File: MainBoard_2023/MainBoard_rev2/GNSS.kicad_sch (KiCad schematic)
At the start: 12 parts

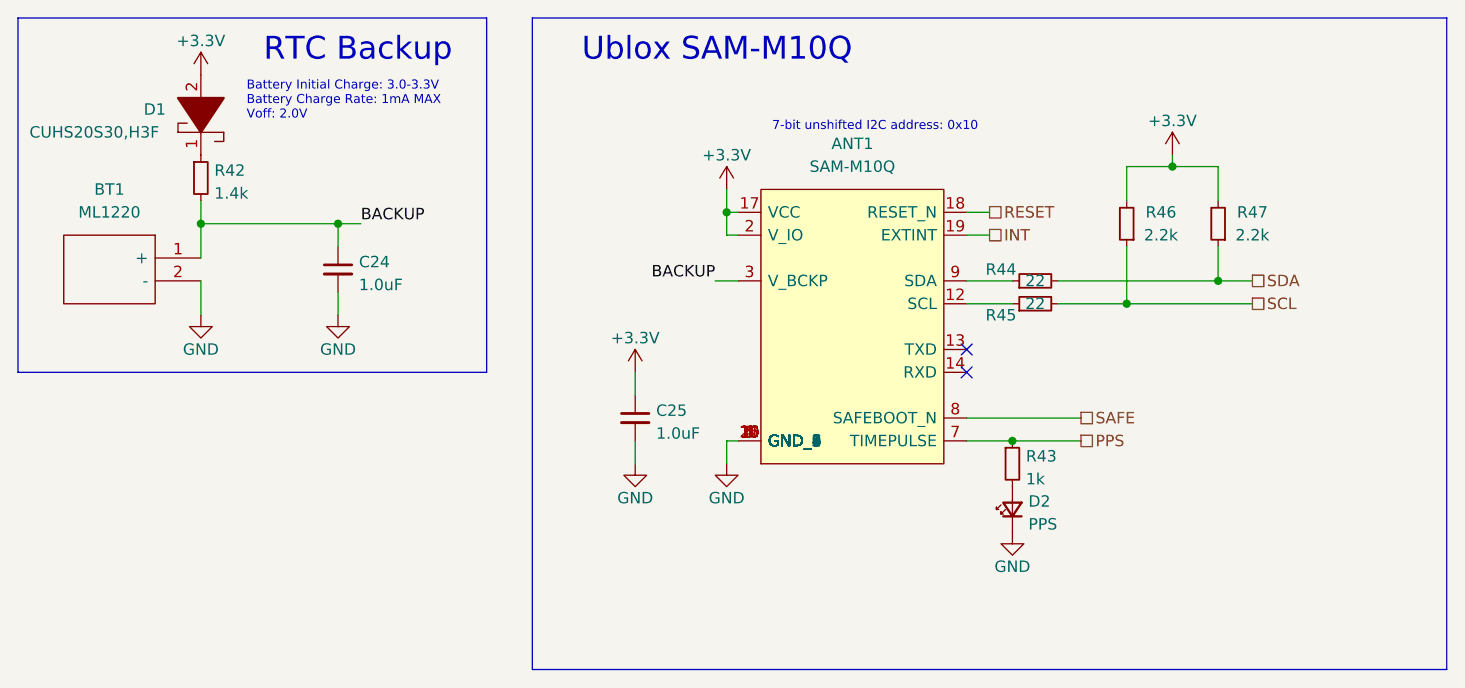
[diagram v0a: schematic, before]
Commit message: PCBファイルを作成
3Dモデルを割り当て　ブロックタイプエミフィルのパッドを小さくした
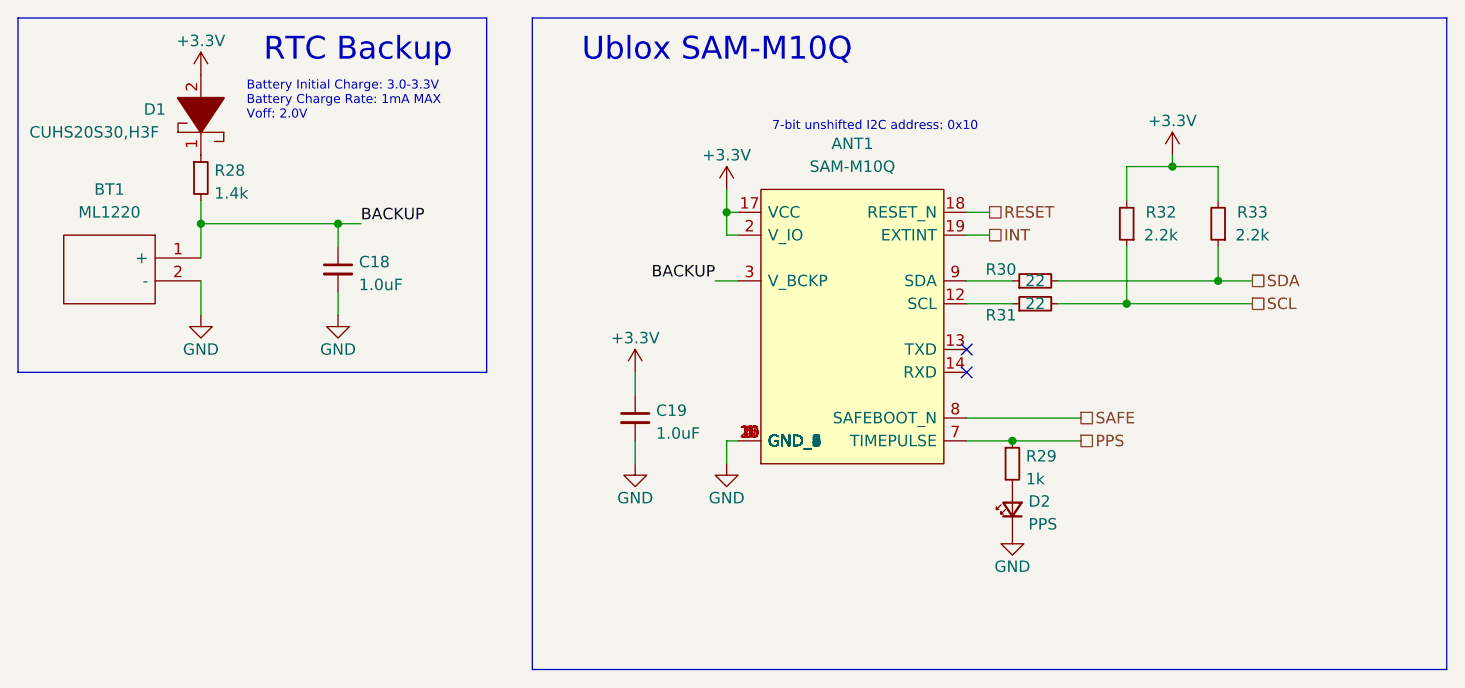
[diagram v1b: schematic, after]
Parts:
- renumbered C24 to C18, C25 to C19, R42 to R28, R43 to R29, R44 to R30, R45 to R31, R46 to R32, R47 to R33
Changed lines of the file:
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@@
   (symbol (lib_id "power:+3.3V") (at 195.58 72.39 0) (unit 1)
     (in_bom yes) (on_board yes)
-    (property "Reference" "#PWR0127" (id 0) (at 195.58 76.2 0)
+    (property "Reference" "#PWR084" (id 0) (at 195.58 76.2 0)
       (effects (font (size 1.27 1.27)) hide)
     )
@@
   (symbol (lib_id "Device:R_Small") (at 180.34 88.9 90) (unit 1)
     (in_bom yes) (on_board yes)
-    (property "Reference" "R45" (id 0) (at 176.53 90.17 90))
+    (property "Reference" "R31" (id 0) (at 176.53 90.17 90))
     (property "Value" "22" (id 1) (at 180.34 88.9 90))
     (property "Footprint" "Resistor_SMD:R_0603_1608Metric_Pad0.98x0.95mm_HandSolder" (id 2) (at 180.34 88.9 0)
@@
   (symbol (lib_id "power:+3.3V") (at 135.89 96.52 0) (unit 1)
     (in_bom yes) (on_board yes)
-    (property "Reference" "#PWR0122" (id 0) (at 135.89 100.33 0)
+    (property "Reference" "#PWR079" (id 0) (at 135.89 100.33 0)
       (effects (font (size 1.27 1.27)) hide)
     )
@@
   (symbol (lib_id "Device:R_Small") (at 200.66 80.01 180) (unit 1)
     (in_bom yes) (on_board yes)
-    (property "Reference" "R47" (id 0) (at 204.47 78.74 0))
+    (property "Reference" "R33" (id 0) (at 204.47 78.74 0))
     (property "Value" "2.2k" (id 1) (at 204.47 81.28 0))
     (property "Footprint" "Resistor_SMD:R_0603_1608Metric_Pad0.98x0.95mm_HandSolder" (id 2) (at 200.66 80.01 0)
@@
   (symbol (lib_id "power:GND") (at 135.89 106.68 0) (unit 1)
     (in_bom yes) (on_board yes)
-    (property "Reference" "#PWR0123" (id 0) (at 135.89 113.03 0)
+    (property "Reference" "#PWR080" (id 0) (at 135.89 113.03 0)
       (effects (font (size 1.27 1.27)) hide)
     )
@@
   (symbol (lib_id "Device:C_Small") (at 135.89 101.6 0) (unit 1)
     (in_bom yes) (on_board yes) (fields_autoplaced)
-    (property "Reference" "C25" (id 0) (at 138.2141 100.7716 0)
+    (property "Reference" "C19" (id 0) (at 138.2141 100.7716 0)
       (effects (font (size 1.27 1.27)) (justify left))
     )
@@
   (symbol (lib_id "Device:C_Small") (at 102.87 85.09 0) (unit 1)
     (in_bom yes) (on_board yes) (fields_autoplaced)
-    (property "Reference" "C24" (id 0) (at 105.1941 84.2616 0)
+    (property "Reference" "C18" (id 0) (at 105.1941 84.2616 0)
       (effects (font (size 1.27 1.27)) (justify left))
     )
@@
   (symbol (lib_id "power:+3.3V") (at 146.05 76.2 0) (unit 1)
     (in_bom yes) (on_board yes)
-    (property "Reference" "#PWR0124" (id 0) (at 146.05 80.01 0)
+    (property "Reference" "#PWR081" (id 0) (at 146.05 80.01 0)
       (effects (font (size 1.27 1.27)) hide)
     )
@@
   (symbol (lib_id "power:GND") (at 177.8 114.3 0) (unit 1)
     (in_bom yes) (on_board yes)
-    (property "Reference" "#PWR0126" (id 0) (at 177.8 120.65 0)
+    (property "Reference" "#PWR083" (id 0) (at 177.8 120.65 0)
       (effects (font (size 1.27 1.27)) hide)
     )
@@
   (symbol (lib_id "Device:R_Small") (at 87.63 74.93 0) (unit 1)
     (in_bom yes) (on_board yes) (fields_autoplaced)
-    (property "Reference" "R42" (id 0) (at 89.1286 74.0953 0)
+    (property "Reference" "R28" (id 0) (at 89.1286 74.0953 0)
       (effects (font (size 1.27 1.27)) (justify left))
     )
@@
   (symbol (lib_id "power:GND") (at 87.63 90.17 0) (unit 1)
     (in_bom yes) (on_board yes)
-    (property "Reference" "#PWR0120" (id 0) (at 87.63 96.52 0)
+    (property "Reference" "#PWR077" (id 0) (at 87.63 96.52 0)
       (effects (font (size 1.27 1.27)) hide)
     )
@@
   (symbol (lib_id "power:GND") (at 146.05 106.68 0) (unit 1)
     (in_bom yes) (on_board yes)
-    (property "Reference" "#PWR0125" (id 0) (at 146.05 113.03 0)
+    (property "Reference" "#PWR082" (id 0) (at 146.05 113.03 0)
       (effects (font (size 1.27 1.27)) hide)
     )
@@
   (symbol (lib_id "Device:R_Small") (at 177.8 106.68 0) (unit 1)
     (in_bom yes) (on_board yes) (fields_autoplaced)
-    (property "Reference" "R43" (id 0) (at 179.2986 105.8453 0)
+    (property "Reference" "R29" (id 0) (at 179.2986 105.8453 0)
       (effects (font (size 1.27 1.27)) (justify left))
     )
@@
   (symbol (lib_id "Device:R_Small") (at 180.34 86.36 90) (unit 1)
     (in_bom yes) (on_board yes)
-    (property "Reference" "R44" (id 0) (at 176.53 85.09 90))
+    (property "Reference" "R30" (id 0) (at 176.53 85.09 90))
     (property "Value" "22" (id 1) (at 180.34 86.36 90))
     (property "Footprint" "Resistor_SMD:R_0603_1608Metric_Pad0.98x0.95mm_HandSolder" (id 2) (at 180.34 86.36 0)
@@
   (symbol (lib_id "Device:R_Small") (at 190.5 80.01 180) (unit 1)
     (in_bom yes) (on_board yes)
-    (property "Reference" "R46" (id 0) (at 194.31 78.74 0))
+    (property "Reference" "R32" (id 0) (at 194.31 78.74 0))
     (property "Value" "2.2k" (id 1) (at 194.31 81.28 0))
     (property "Footprint" "Resistor_SMD:R_0603_1608Metric_Pad0.98x0.95mm_HandSolder" (id 2) (at 190.5 80.01 0)
@@
   (symbol (lib_id "power:GND") (at 102.87 90.17 0) (unit 1)
     (in_bom yes) (on_board yes)
-    (property "Reference" "#PWR0121" (id 0) (at 102.87 96.52 0)
+    (property "Reference" "#PWR078" (id 0) (at 102.87 96.52 0)
       (effects (font (size 1.27 1.27)) hide)
     )
@@
   (symbol (lib_id "power:+3.3V") (at 87.63 63.5 0) (unit 1)
     (in_bom yes) (on_board yes)
-    (property "Reference" "#PWR0119" (id 0) (at 87.63 67.31 0)
-      (effects (font (size 1.27 1.27)) hide)
-    )
+    (property "Reference" "#PWR076" (id 0) (at 87.63 67.31 0)
+      (effects (font (size 1.27 1.27)) hide)
+    )
